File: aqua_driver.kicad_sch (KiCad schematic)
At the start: 0 parts

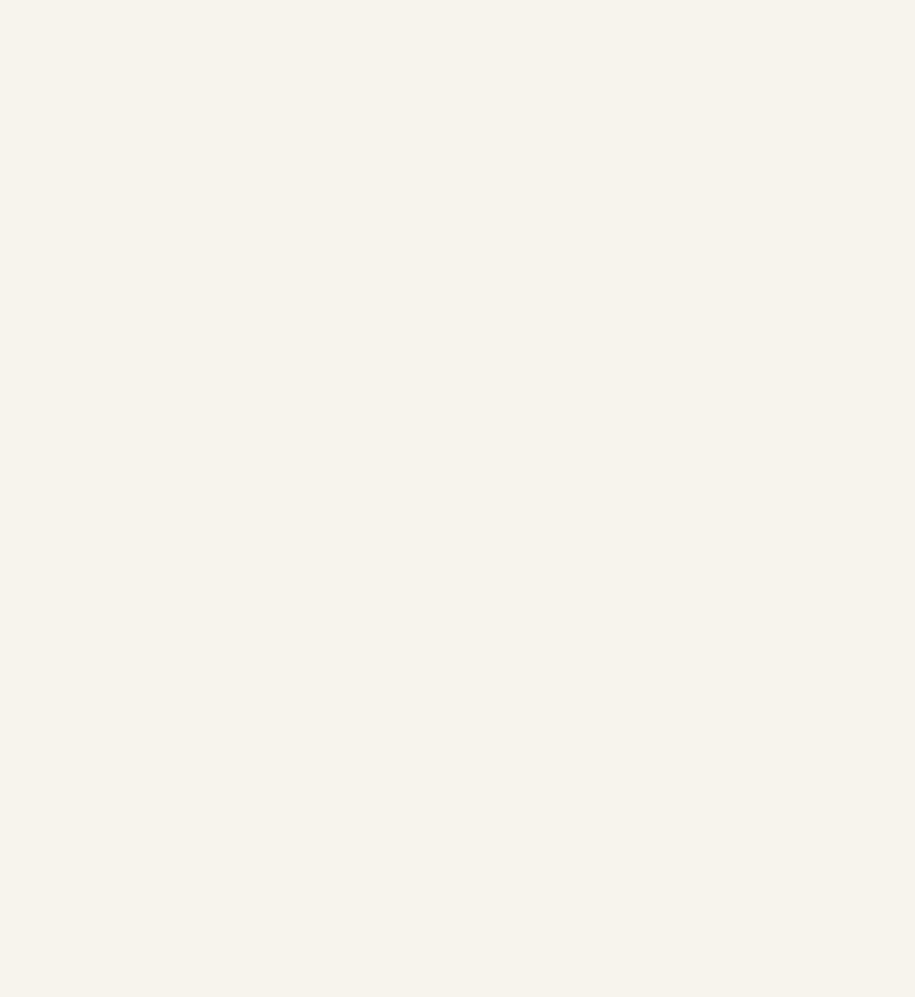
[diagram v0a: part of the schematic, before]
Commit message: First additions to project (#1)
* Added/Updated KiCAD project files.
Added 230V connectors to schematic.
Added basic relay circuit to schematic.
Added .gitignore file.

* Fixed floating point in config.

* Round numbers

---------

Co-authored-by: Sławomir Kozok <slawomir.kozok@3dgence.com>
Co-authored-by: Michał Walenciak <Kicer86@gmail.com>
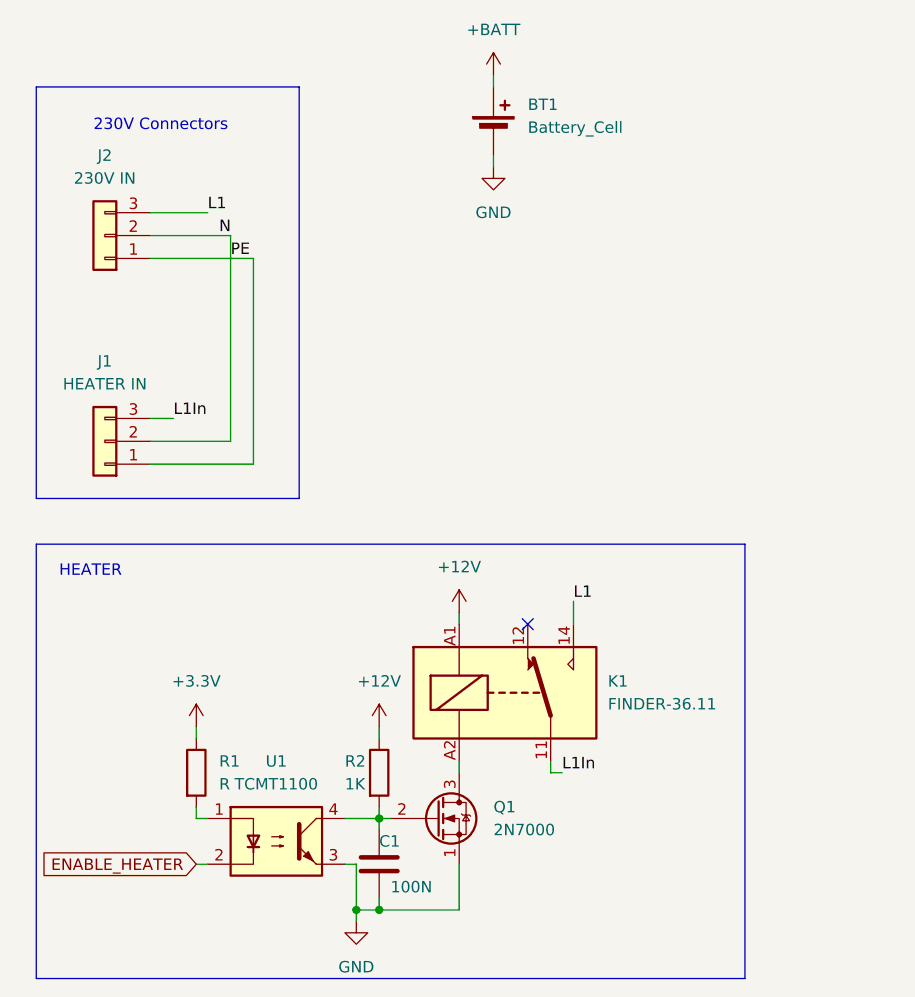
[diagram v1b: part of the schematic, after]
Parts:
- added BT1: Battery_Cell, symbol Device:Battery_Cell
- added C1: 100N, symbol Device:C
- added J1: HEATER IN, symbol Connector_Generic:Conn_01x03
- added J2: 230V IN, symbol Connector_Generic:Conn_01x03
- added K1: FINDER-36.11, Relay_THT:Relay_SPDT_Finder_36.11, symbol Relay:FINDER-36.11
- added Q1: 2N7000, Package_TO_SOT_THT:TO-92_Inline, symbol Transistor_FET:2N7000
- added R1: R, symbol Device:R
- added R2: 1K, symbol Device:R
- added U1: TCMT1100, Package_SO:SOP-4_4.4x2.6mm_P1.27mm, symbol Isolator:TCMT1100
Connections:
- new net: K1.A2, Q1.3 (D)
- new net: C1.1, Q1.2 (G), R2.2, U1.4
- new net: R1.2, U1.1
- new net +12V: K1.A1, R2.1
- new net +3.3V: R1.1
- new net +BATT: BT1.1 (+)
- new net ENABLE_HEATER: U1.2
- new net GND: BT1.2 (-), C1.2, Q1.1 (S), U1.3
- new net L1: J2.3 (Pin_3), K1.14
- new net L1In: J1.3 (Pin_3), K1.11
- new net N: J1.1 (Pin_1), J1.2 (Pin_2), J2.1 (Pin_1), J2.2 (Pin_2)
- no-connect marks 0 -> 1
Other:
- note added: "230V Connectors"
- note added: "HEATER"

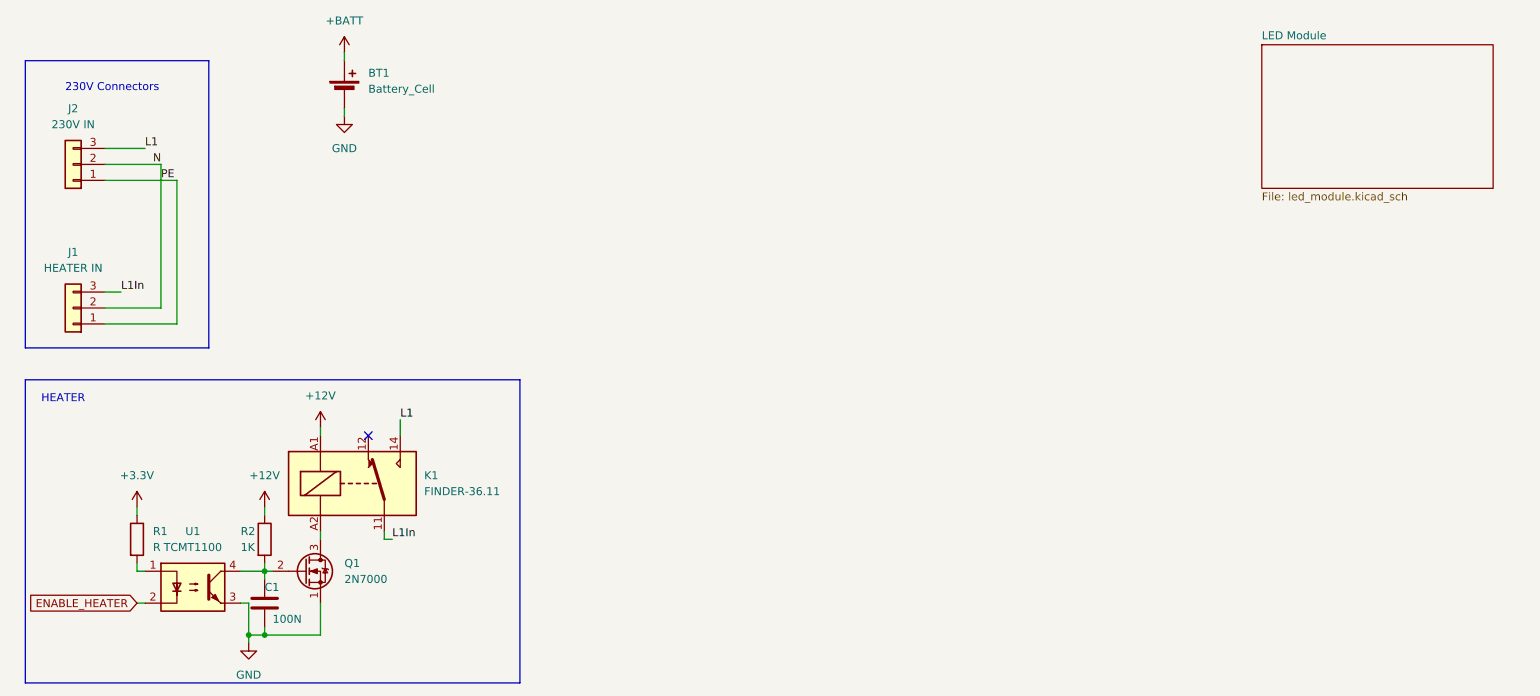
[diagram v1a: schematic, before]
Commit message: Move heater into temperature control sheet
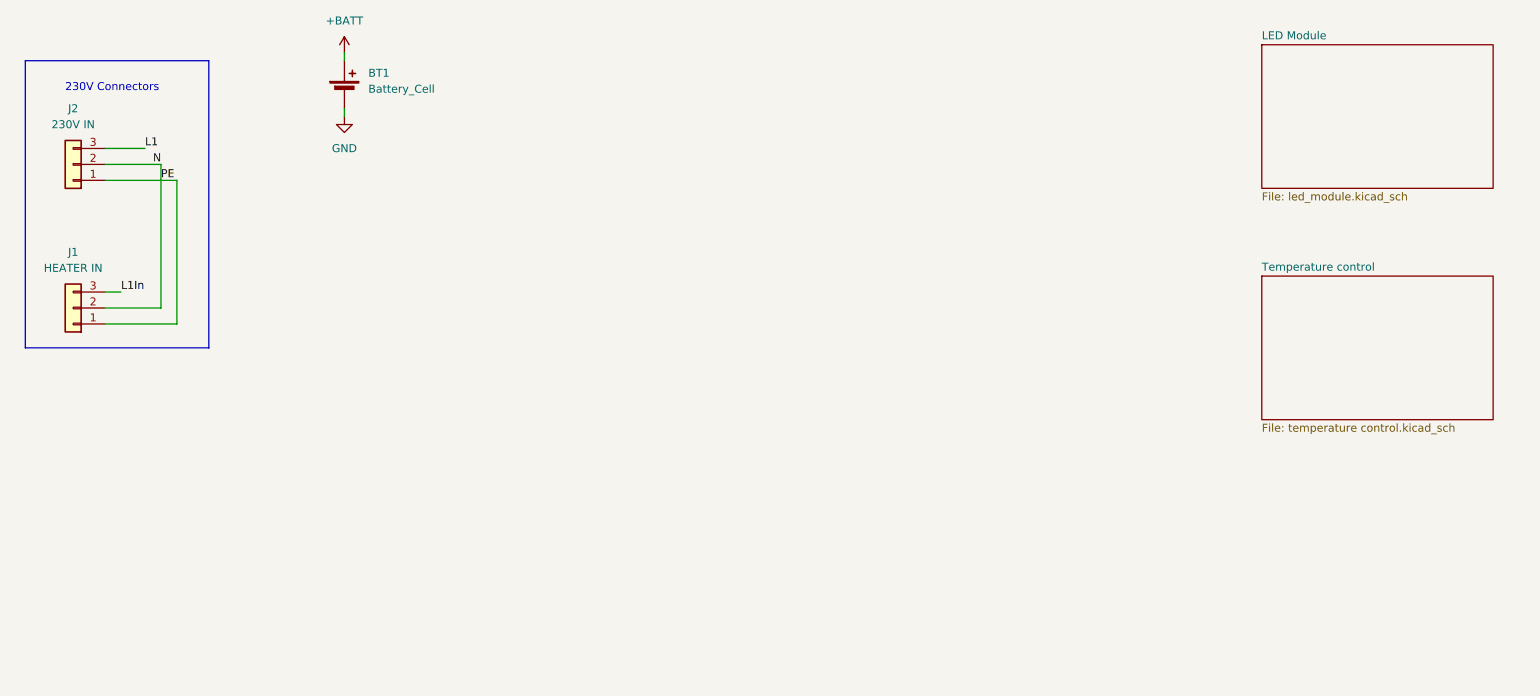
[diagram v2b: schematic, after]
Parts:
- removed C1: 100N, symbol Device:C
- removed K1: FINDER-36.11, Relay_THT:Relay_SPDT_Finder_36.11, symbol Relay:FINDER-36.11
- removed Q1: 2N7000, Package_TO_SOT_THT:TO-92_Inline, symbol Transistor_FET:2N7000
- removed R1: R, symbol Device:R
- removed R2: 1K, symbol Device:R
- removed U1: TCMT1100, Package_SO:SOP-4_4.4x2.6mm_P1.27mm, symbol Isolator:TCMT1100
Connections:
- no-connect marks 1 -> 0
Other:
- added sheet Temperature control (temperature control.kicad_sch)
- note removed: "HEATER"
